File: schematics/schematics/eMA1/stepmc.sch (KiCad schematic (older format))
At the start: 14 parts, among them IC1 PIC16F1824, IC2 L298, P1 CONN_4, P2 CONN_4, P3 CONN_6, P4 CONN_4

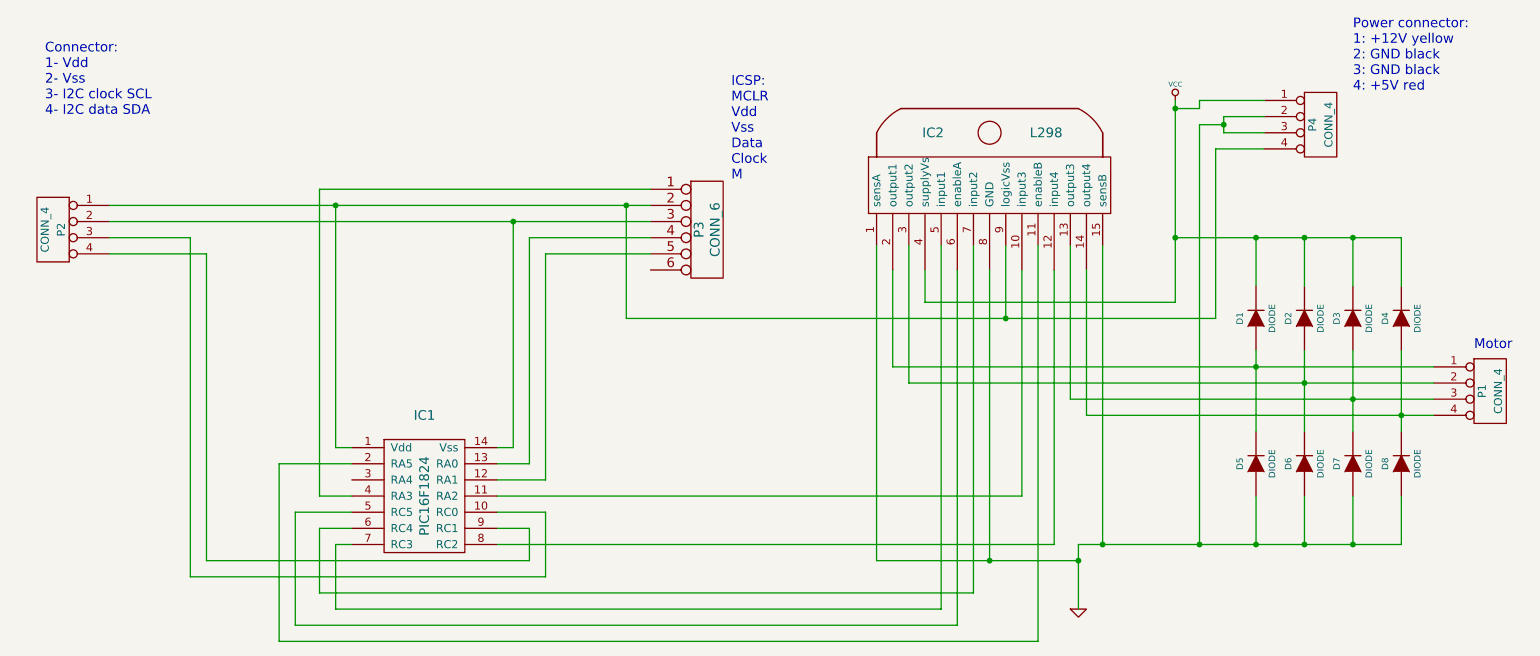
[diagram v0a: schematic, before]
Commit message: eMA1 netlist and board (no routing yet)
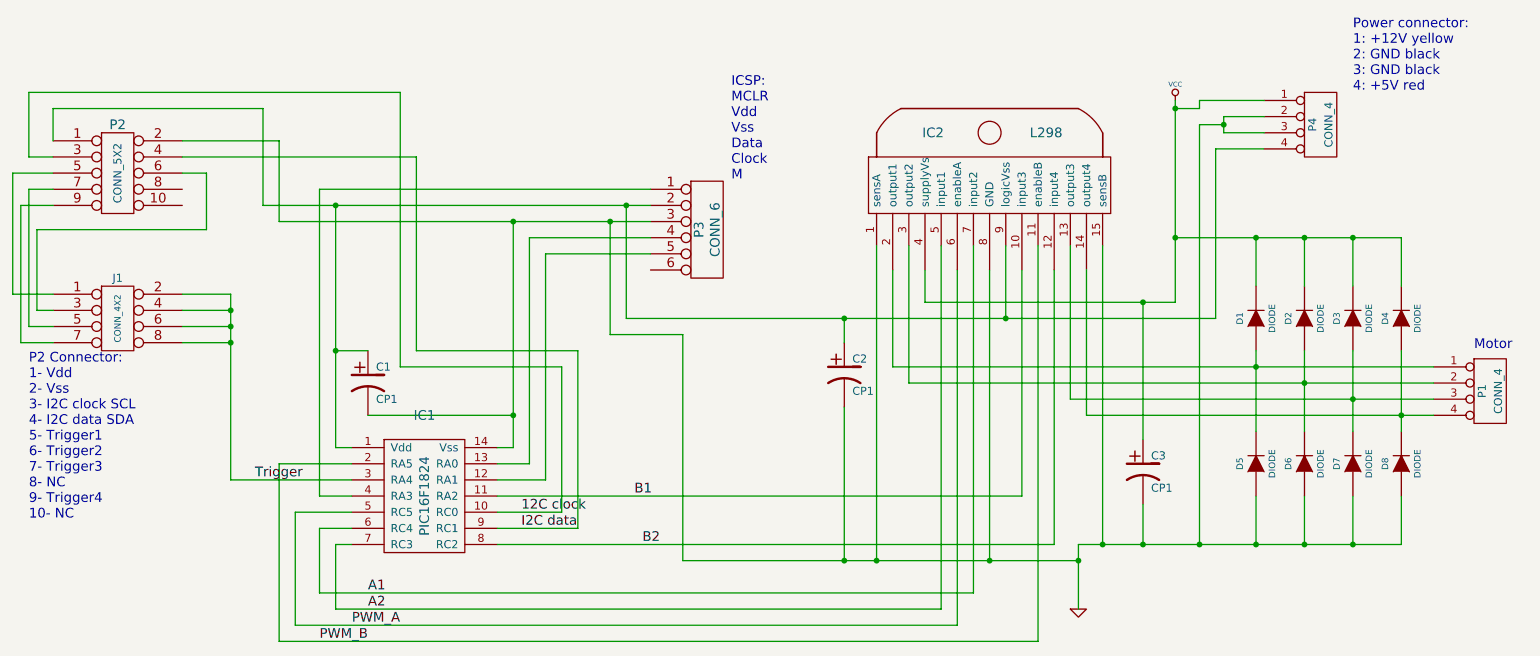
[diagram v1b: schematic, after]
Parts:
- removed P2: CONN_4, symbol CONN_4
- added C1, C2, C3: CP1, symbol CP1
- added J1: CONN_4X2, symbol CONN_4X2
- added P2: CONN_5X2, symbol CONN_5X2
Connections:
- net GND: now also IC1.14 (Vss), P3.3, C1.2, C2.2, C3.2, P2.2
- net VCC: now also C3.1
- net B1: now reaches IC1.11 (RA2), IC2.10 (input3)
- net PWM_B: now reaches IC1.2 (RA5), IC2.11 (enableB)
- net B2: now reaches IC1.8 (RC2), IC2.12 (input4)
- net A2: now reaches IC1.7 (RC3), IC2.5 (input1)
- net PWM_A: now reaches IC1.5 (RC5), IC2.6 (enableA)
- net A1: now reaches IC1.6 (RC4), IC2.7 (input2)
- net at IC1.1 (Vdd), IC2.9 (logicVss), P3.2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: now also C1.1, C2.1, P2.1
- net 12C clock: now reaches IC1.10 (RC0)
- net 12C clock: now also P2.3
- net Trigger: now reaches IC1.3 (RA4)
- net Trigger: now also J1.2, J1.4, J1.6, J1.8
- net I2C data: now reaches IC1.9 (RC1)
- net I2C data: now also P2.4
- new net: J1.1, P2.5
- new net: J1.3, P2.6
- new net: J1.5, P2.7
- new net: J1.7, P2.9
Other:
- note added: "P2 Connector:\n1- Vdd\n2- Vss\n3- I2C clock SCL\n4- I2C data SDA\n5- Trigger1\n6- Trigger2\n7- Trigger3\n8- NC\n9- Trigger4\n10- NC"
- note removed: "Connector:\n1- Vdd\n2- Vss\n3- I2C clock SCL\n4- I2C data SDA"
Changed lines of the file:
@@
-EESchema Schematic File Version 2  date 2012. 01. 31. 16:14:08
+EESchema Schematic File Version 2  date 2012. 02. 17. 15:43:41
 LIBS:pic16f1824
 LIBS:power
@@
 Sheet 1 1
 Title "Stepper motor control circuit"
-Date "31 jan 2012"
+Date "17 feb 2012"
 Rev "1"
 Comp ""
@@
 Comment4 ""
 $EndDescr
+Wire Wire Line
+	3600 3500 4100 3500
+Connection ~ 7600 2100
+Wire Wire Line
+	7600 2950 7600 2100
+Connection ~ 5750 2200
+Wire Wire Line
+	5750 2350 5750 2200
+Connection ~ 2600 2400
+Wire Wire Line
+	2600 2400 2800 2400
+Connection ~ 1950 2350
+Wire Wire Line
+	1650 2350 1950 2350
+Connection ~ 1950 2150
+Wire Wire Line
+	1650 2150 1950 2150
+Wire Wire Line
+	850  1500 650  1500
+Wire Wire Line
+	650  1500 650  2350
+Wire Wire Line
+	650  2350 850  2350
+Wire Wire Line
+	850  1400 700  1400
+Wire Wire Line
+	850  1300 600  1300
+Wire Wire Line
+	600  1300 600  2050
+Wire Wire Line
+	600  2050 850  2050
+Wire Wire Line
+	850  1200 700  1200
+Wire Wire Line
+	700  1200 700  800
+Wire Wire Line
+	700  800  3000 800
+Wire Wire Line
+	3000 800  3000 2500
+Wire Wire Line
+	3000 2500 4000 2500
+Wire Wire Line
+	4000 2500 4000 3400
+Wire Wire Line
+	4000 3400 3600 3400
 Connection ~ 6750 2200
 Wire Wire Line
@@
 	2350 3400 2700 3400
 Wire Wire Line
-	1200 1800 1800 1800
-Wire Wire Line
-	1800 1800 1800 3700
-Wire Wire Line
-	1800 3700 3800 3700
-Wire Wire Line
-	3800 3700 3800 3500
-Wire Wire Line
-	3800 3500 3600 3500
-Wire Wire Line
 	4550 1800 3900 1800
 Wire Wire Line
@@
 	2600 3000 2700 3000
 Wire Wire Line
-	1200 1500 4550 1500
-Wire Wire Line
-	7200 3700 5950 3700
-Wire Wire Line
 	5950 3700 5950 1750
 Wire Wire Line
-	6650 3700 6650 1900
+	6650 1900 6650 3700
 Connection ~ 6650 3700
 Connection ~ 7200 3700
@@
 Connection ~ 8900 3600
 Wire Wire Line
-	8300 3300 8300 3600
+	8300 3600 8300 3300
 Connection ~ 8300 3600
 Wire Wire Line
@@
 Connection ~ 7350 3600
 Wire Wire Line
-	4550 1600 1200 1600
-Wire Wire Line
 	3600 3000 3700 3000
 Wire Wire Line
@@
 	3800 1700 4550 1700
 Wire Wire Line
-	3600 3400 3900 3400
-Wire Wire Line
-	3900 3400 3900 3800
-Wire Wire Line
-	3900 3800 1700 3800
-Wire Wire Line
-	1700 3800 1700 1700
-Wire Wire Line
-	1700 1700 1200 1700
-Wire Wire Line
-	6750 2200 6750 1750
+	6750 1750 6750 2200
 Wire Wire Line
 	4400 2200 4400 1500
@@
 Wire Wire Line
 	8100 1050 8350 1050
+Wire Wire Line
+	4550 1500 2150 1500
+Wire Wire Line
+	2150 1500 2150 900
+Wire Wire Line
+	2150 900  850  900
+Wire Wire Line
+	850  900  850  1100
+Wire Wire Line
+	4550 1600 2250 1600
+Wire Wire Line
+	2250 1600 2250 1100
+Wire Wire Line
+	2250 1100 1650 1100
+Wire Wire Line
+	4100 3500 4100 2400
+Wire Wire Line
+	4100 2400 3100 2400
+Wire Wire Line
+	3100 2400 3100 1200
+Wire Wire Line
+	3100 1200 1650 1200
+Wire Wire Line
+	850  2150 750  2150
+Wire Wire Line
+	750  2150 750  1650
+Wire Wire Line
+	750  1650 1800 1650
+Wire Wire Line
+	1800 1650 1800 1300
+Wire Wire Line
+	1800 1300 1650 1300
+Wire Wire Line
+	850  2250 700  2250
+Wire Wire Line
+	700  2250 700  1400
+Wire Wire Line
+	1650 2050 1950 2050
+Wire Wire Line
+	1950 2050 1950 3200
+Wire Wire Line
+	1950 3200 2700 3200
+Wire Wire Line
+	1650 2250 1950 2250
+Connection ~ 1950 2250
+Wire Wire Line
+	7200 3700 4750 3700
+Wire Wire Line
+	4750 3700 4750 2300
+Wire Wire Line
+	4750 2300 4300 2300
+Wire Wire Line
+	4300 2300 4300 1600
+Connection ~ 4300 1600
+Connection ~ 5950 3700
+Wire Wire Line
+	2800 2800 3700 2800
+Connection ~ 3700 2800
+Wire Wire Line
+	5750 2750 5750 3700
+Connection ~ 5750 3700
+Wire Wire Line
+	7600 3350 7600 3600
+Connection ~ 7600 3600
+$Comp
+L CP1 C3
+U 1 1 4F3E63C2
+P 7600 3150
+F 0 "C3" H 7650 3250 50  0000 L CNN
+F 1 "CP1" H 7650 3050 50  0000 L CNN
+	1    7600 3150
+	1    0    0    -1
+$EndComp
+$Comp
+L CP1 C2
+U 1 1 4F3E63B9
+P 5750 2550
+F 0 "C2" H 5800 2650 50  0000 L CNN
+F 1 "CP1" H 5800 2450 50  0000 L CNN
+	1    5750 2550
+	1    0    0    -1
+$EndComp
+$Comp
+L CP1 C1
+U 1 1 4F3E6398
+P 2800 2600
+F 0 "C1" H 2850 2700 50  0000 L CNN
+F 1 "CP1" H 2850 2500 50  0000 L CNN
+	1    2800 2600
+	1    0    0    -1
+$EndComp
+Text Label 4500 3600 0    60   ~ 0
+B2
+Text Label 4450 3300 0    60   ~ 0
+B1
+Text Label 2800 4000 0    60   ~ 0
+A2
+Text Label 2800 3900 0    60   ~ 0
+A1
+Text Label 2100 3200 0    60   ~ 0
+Trigger
+$Comp
+L CONN_4X2 J1
+U 1 1 4F3E5882
+P 1250 2200
+F 0 "J1" H 1250 2450 50  0000 C CNN
+F 1 "CONN_4X2" V 1250 2200 40  0000 C CNN
+	1    1250 2200
+	1    0    0    -1
+$EndComp
+Text Label 2500 4200 0    60   ~ 0
+PWM_B
+Text Label 2700 4100 0    60   ~ 0
+PWM_A
+Text Label 3750 3400 0    60   ~ 0
+12C clock
+Text Label 3750 3500 0    60   ~ 0
+I2C data
+$Comp
+L CONN_5X2 P2
+U 1 1 4F3E5590
+P 1250 1300
+F 0 "P2" H 1250 1600 60  0000 C CNN
+F 1 "CONN_5X2" V 1250 1300 50  0000 C CNN
+	1    1250 1300
+	1    0    0    -1
+$EndComp
 Text Notes 8900 800  0    60   ~ 0
 Power connector:\n1: +12V yellow\n2: GND black\n3: GND black\n4: +5V red\n
@@
 $EndComp
 $Comp
-L CONN_4 P2
-U 1 1 4F27CE3D
-P 850 1650
-F 0 "P2" V 800 1650 50  0000 C CNN
-F 1 "CONN_4" V 900 1650 50  0000 C CNN
-	1    850  1650
-	-1   0    0    -1
-$EndComp
-$Comp
 L PIC16F1824 IC1
 U 1 1 4F27CD9A
@@
 	1    0    0    -1
 $EndComp
-Text Notes 800  950  0    60   ~ 0
-Connector:\n1- Vdd\n2- Vss\n3- I2C clock SCL\n4- I2C data SDA
-$Comp
-L GND #PWR?
+Text Notes 700  3450 0    60   ~ 0
+P2 Connector:\n1- Vdd\n2- Vss\n3- I2C clock SCL\n4- I2C data SDA\n5- Trigger1\n6- Trigger2\n7- Trigger3\n8- NC\n9- Trigger4\n10- NC
+$Comp
+L GND #PWR01
 U 1 1 4F0C8891
 P 7200 4000
-F 0 "#PWR?" H 7200 4000 30  0001 C CNN
+F 0 "#PWR01" H 7200 4000 30  0001 C CNN
 F 1 "GND" H 7200 3930 30  0001 C CNN
 	1    7200 4000
@@
 $EndComp
 $Comp
-L VCC #PWR?
+L VCC #PWR02
 U 1 1 4F0C887F
 P 7800 850
-F 0 "#PWR?" H 7800 950 30  0001 C CNN
+F 0 "#PWR02" H 7800 950 30  0001 C CNN
 F 1 "VCC" H 7800 950 30  0000 C CNN
 	1    7800 850
